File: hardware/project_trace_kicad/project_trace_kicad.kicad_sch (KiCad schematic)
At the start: 0 parts

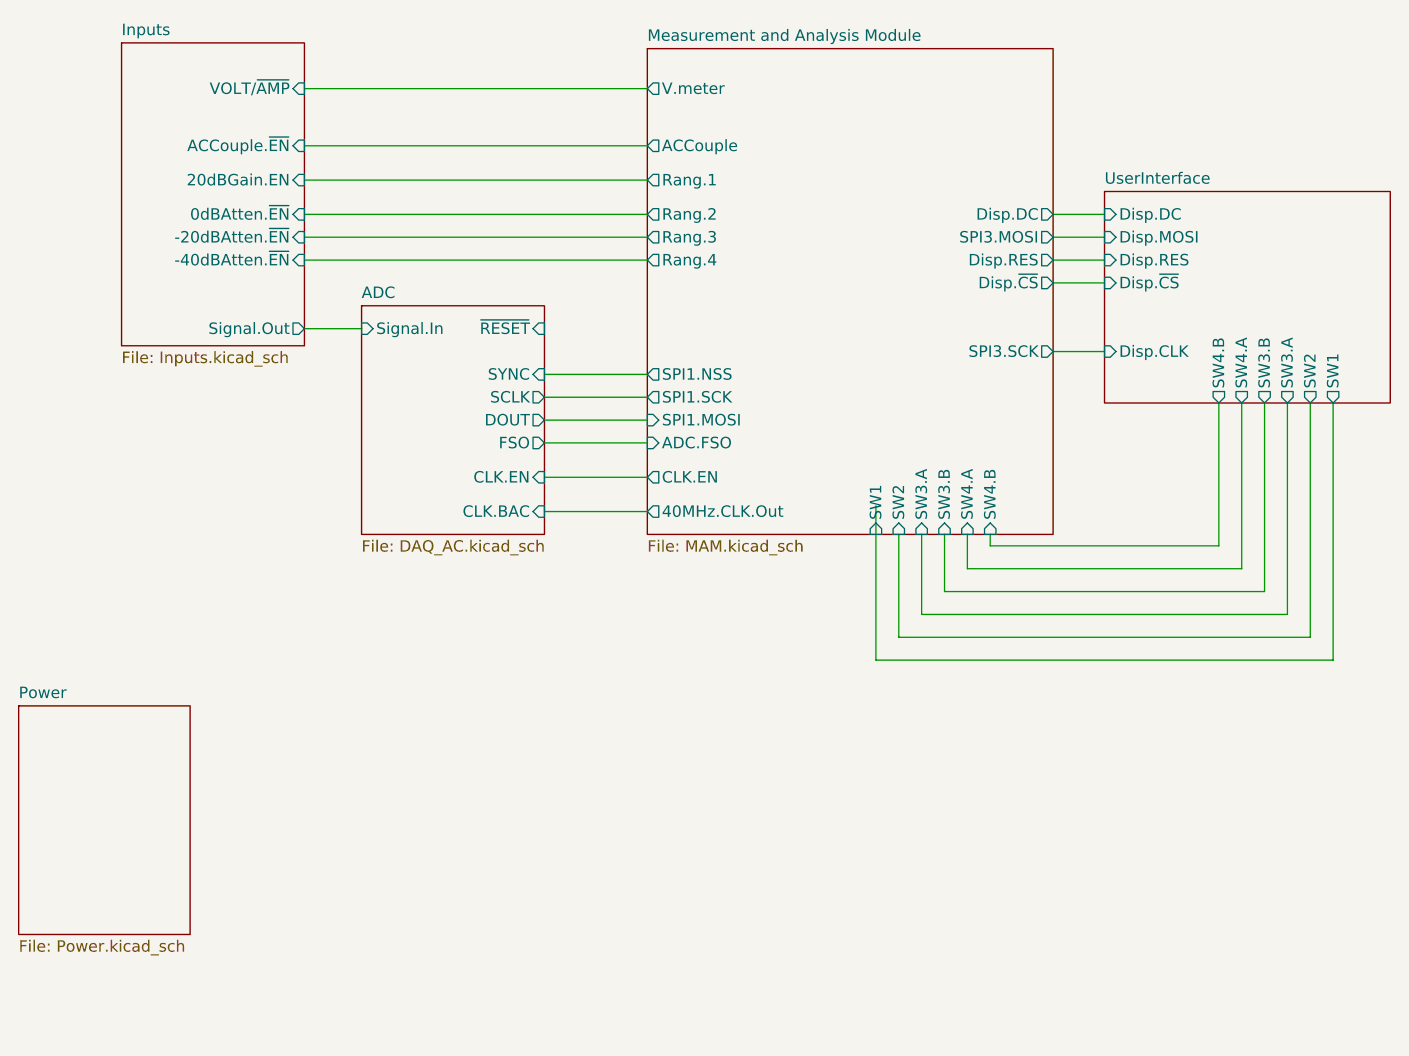
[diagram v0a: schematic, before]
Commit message: ERC Checks & Bug-Fixing
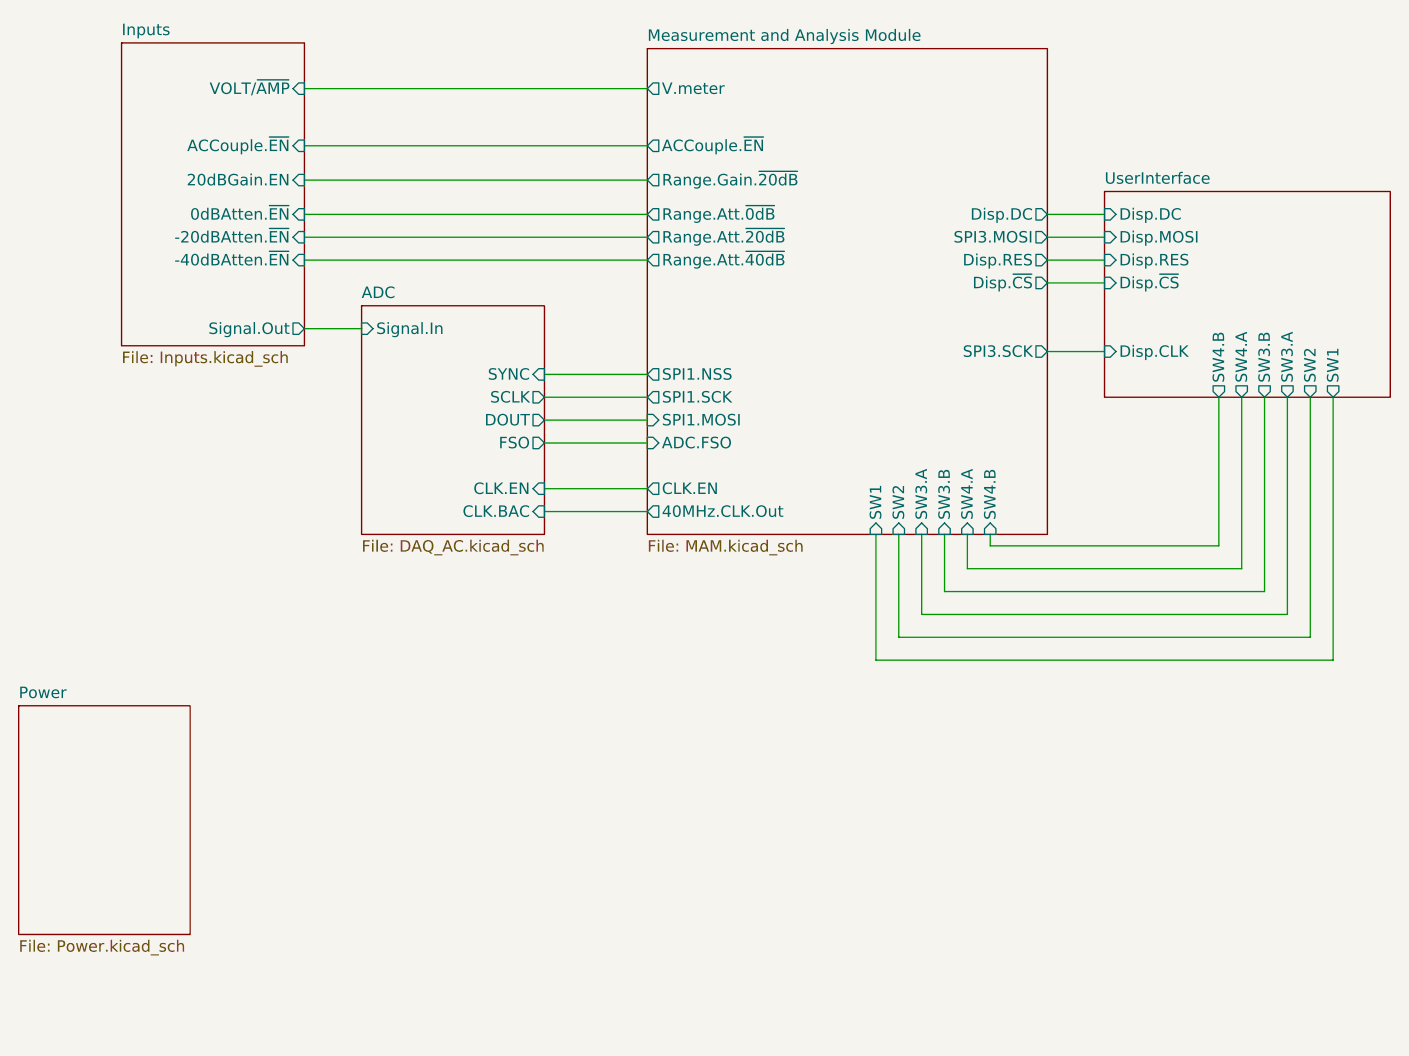
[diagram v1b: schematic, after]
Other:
- sheet ADC ports: added none; removed ~{RESET}
- sheet Measurement and Analysis Module ports: added ACCouple.~{EN}, Range.Att.~{0dB}, Range.Att.~{20dB}, Range.Att.~{40dB}, Range.Gain.~{20dB}; removed ACCouple, Rang.1, Rang.2, Rang.3, Rang.4
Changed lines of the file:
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@@
 	(wire
 		(pts
-			(xy 146.05 98.425) (xy 146.05 115.57)
-		)
-		(stroke
-			(width 0)
-			(type default)
-		)
-	)
-	(wire
-		(pts
-			(xy 109.22 95.25) (xy 120.65 95.25)
-		)
-		(stroke
-			(width 0)
-			(type default)
-		)
-	)
-	(wire
-		(pts
-			(xy 186.69 86.995) (xy 186.69 105.41)
+			(xy 146.05 101.6) (xy 146.05 115.57)
+		)
+		(stroke
+			(width 0)
+			(type default)
+		)
+	)
+	(wire
+		(pts
+			(xy 109.22 96.52) (xy 120.65 96.52)
+		)
+		(stroke
+			(width 0)
+			(type default)
+		)
+	)
+	(wire
+		(pts
+			(xy 186.69 86.36) (xy 186.69 105.41)
 		)
 		(stroke
@@
 	(wire
 		(pts
-			(xy 194.31 86.995) (xy 194.31 113.03)
+			(xy 194.31 86.36) (xy 194.31 113.03)
 		)
 		(stroke
@@
 	(wire
 		(pts
-			(xy 196.85 86.995) (xy 196.85 115.57)
-		)
-		(stroke
-			(width 0)
-			(type default)
-		)
-	)
-	(wire
-		(pts
-			(xy 165.735 81.28) (xy 171.45 81.28)
-		)
-		(stroke
-			(width 0)
-			(type default)
-		)
-	)
-	(wire
-		(pts
-			(xy 165.735 73.66) (xy 171.45 73.66)
-		)
-		(stroke
-			(width 0)
-			(type default)
-		)
-	)
-	(wire
-		(pts
-			(xy 191.77 86.995) (xy 191.77 110.49)
+			(xy 196.85 86.36) (xy 196.85 115.57)
+		)
+		(stroke
+			(width 0)
+			(type default)
+		)
+	)
+	(wire
+		(pts
+			(xy 165.1 81.28) (xy 171.45 81.28)
+		)
+		(stroke
+			(width 0)
+			(type default)
+		)
+	)
+	(wire
+		(pts
+			(xy 165.1 73.66) (xy 171.45 73.66)
+		)
+		(stroke
+			(width 0)
+			(type default)
+		)
+	)
+	(wire
+		(pts
+			(xy 191.77 86.36) (xy 191.77 110.49)
 		)
 		(stroke
@@
 	(wire
 		(pts
-			(xy 165.735 66.04) (xy 171.45 66.04)
+			(xy 165.1 66.04) (xy 171.45 66.04)
 		)
 		(stroke
@@
 	(wire
 		(pts
-			(xy 184.15 86.995) (xy 184.15 102.87)
+			(xy 184.15 86.36) (xy 184.15 102.87)
 		)
 		(stroke
@@
 	(wire
 		(pts
-			(xy 165.735 71.12) (xy 171.45 71.12)
-		)
-		(stroke
-			(width 0)
-			(type default)
-		)
-	)
-	(wire
-		(pts
-			(xy 165.735 68.58) (xy 171.45 68.58)
+			(xy 165.1 71.12) (xy 171.45 71.12)
+		)
+		(stroke
+			(width 0)
+			(type default)
+		)
+	)
+	(wire
+		(pts
+			(xy 165.1 68.58) (xy 171.45 68.58)
 		)
 		(stroke
@@
 	(wire
 		(pts
-			(xy 189.23 86.995) (xy 189.23 107.95)
+			(xy 189.23 86.36) (xy 189.23 107.95)
 		)
 		(stroke
@@
 	(sheet
 		(at 171.45 63.5)
-		(size 31.75 23.495)
+		(size 31.75 22.86)
 		(exclude_from_sim no)
 		(in_bom yes)
@@
 		)
 		(pin "SW1" output
-			(at 196.85 86.995 270)
+			(at 196.85 86.36 270)
 			(effects
 				(font
@@
 		)
 		(pin "SW2" output
-			(at 194.31 86.995 270)
+			(at 194.31 86.36 270)
 			(effects
 				(font
@@
 		)
 		(pin "SW3.A" output
-			(at 191.77 86.995 270)
+			(at 191.77 86.36 270)
 			(effects
 				(font
@@
 		)
 		(pin "SW3.B" output
-			(at 189.23 86.995 270)
+			(at 189.23 86.36 270)
 			(effects
 				(font
@@
 		)
 		(pin "SW4.A" output
-			(at 186.69 86.995 270)
+			(at 186.69 86.36 270)
 			(effects
 				(font
@@
 		)
 		(pin "SW4.B" output
-			(at 184.15 86.995 270)
+			(at 184.15 86.36 270)
 			(effects
 				(font
@@
 			)
 		)
-		(pin "~{RESET}" input
-			(at 109.22 78.74 0)
-			(effects
-				(font
-					(size 1.27 1.27)
-				)
-				(justify right)
-			)
-		)
 		(pin "CLK.BAC" input
 			(at 109.22 99.06 0)
@@
 		)
 		(pin "CLK.EN" input
-			(at 109.22 95.25 0)
+			(at 109.22 96.52 0)
 			(effects
 				(font
@@
 	(sheet
 		(at 120.65 47.625)
-		(size 45.085 53.975)
+		(size 44.45 53.975)
 		(exclude_from_sim no)
 		(in_bom yes)
@@
 		)
 		(pin "Disp.DC" output
-			(at 165.735 66.04 0)
+			(at 165.1 66.04 0)
 			(effects
 				(font
@@
 		)
 		(pin "Disp.RES" output
-			(at 165.735 71.12 0)
+			(at 165.1 71.12 0)
 			(effects
 				(font
@@
 		)
 		(pin "Disp.~{CS}" output
-			(at 165.735 73.66 0)
+			(at 165.1 73.66 0)
 			(effects
 				(font
@@
 		)
 		(pin "SPI3.MOSI" output
-			(at 165.735 68.58 0)
+			(at 165.1 68.58 0)
 			(effects
 				(font
@@
 		)
 		(pin "SPI3.SCK" output
-			(at 165.735 81.28 0)
-			(effects
-				(font
-					(size 1.27 1.27)
-				)
-				(justify right)
-			)
-		)
-		(pin "ACCouple" output
-			(at 120.65 58.42 180)
-			(effects
-				(font
-					(size 1.27 1.27)
-				)
-				(justify left)
-			)
-		)
-		(pin "Rang.1" output
-			(at 120.65 62.23 180)
-			(effects
-				(font
-					(size 1.27 1.27)
-				)
-				(justify left)
-			)
-		)
-		(pin "Rang.2" output
-			(at 120.65 66.04 180)
-			(effects
-				(font
-					(size 1.27 1.27)
-				)
-				(justify left)
-			)
-		)
-		(pin "Rang.3" output
-			(at 120.65 68.58 180)
-			(effects
-				(font
-					(size 1.27 1.27)
-				)
-				(justify left)
-			)
-		)
-		(pin "Rang.4" output
-			(at 120.65 71.12 180)
-			(effects
-				(font
-					(size 1.27 1.27)
-				)
-				(justify left)
+			(at 165.1 81.28 0)
+			(effects
+				(font
+					(size 1.27 1.27)
+				)
+				(justify right)
 			)
 		)
@@
 		)
 		(pin "CLK.EN" output
-			(at 120.65 95.25 180)
-			(effects
-				(font
+			(at 120.65 96.52 180)
+			(effects
+				(font
+					(size 1.27 1.27)
+				)
+				(justify left)
+			)
+		)
+		(pin "ACCouple.~{EN}" output
+			(at 120.65 58.42 180)
+			(effects
+				(font
+					(size 1.27 1.27)
+				)
+				(justify left)
+			)
+		)
+		(pin "Range.Att.~{0dB}" output
+			(at 120.65 66.04 180)
+			(effects
+				(font
+					(size 1.27 1.27)
+				)
+				(justify left)
+			)
+		)
+		(pin "Range.Att.~{20dB}" output
+			(at 120.65 68.58 180)
+			(effects
+				(font
+					(size 1.27 1.27)
+				)
+				(justify left)
+			)
+		)
+		(pin "Range.Att.~{40dB}" output
+			(at 120.65 71.12 180)
+			(effects
+				(font
+					(size 1.27 1.27)
+				)
+				(justify left)
+			)
+		)
+		(pin "Range.Gain.~{20dB}" output
+			(at 120.65 62.23 180)
+			(effects
+				(font

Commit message: Fix inconsistency with ADC datasheet, fix DRC Errors
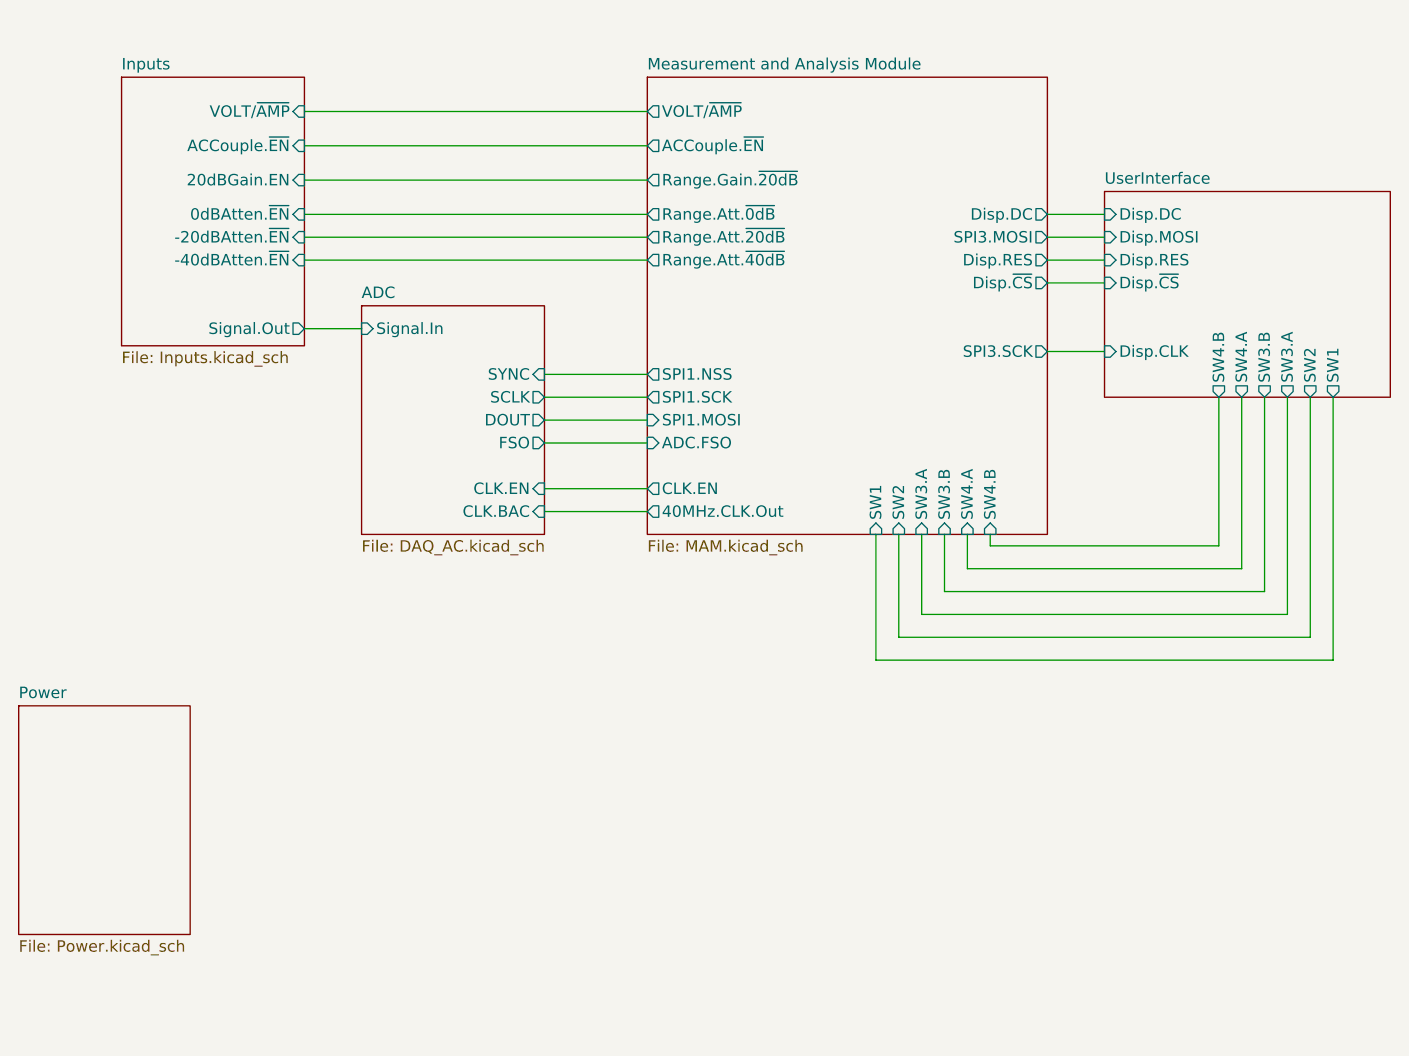
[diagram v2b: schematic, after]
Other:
- sheet Measurement and Analysis Module ports: added VOLT/~{AMP}; removed V.meter
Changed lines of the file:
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@@
 	(wire
 		(pts
-			(xy 82.55 52.07) (xy 120.65 52.07)
+			(xy 82.55 54.61) (xy 120.65 54.61)
 		)
 		(stroke
@@
 	)
 	(sheet
-		(at 62.23 46.99)
-		(size 20.32 33.655)
+		(at 62.23 50.8)
+		(size 20.32 29.845)
 		(exclude_from_sim no)
 		(in_bom yes)
@@
 		)
 		(property "Sheetname" "Inputs"
-			(at 62.23 46.2784 0)
+			(at 62.23 50.0884 0)
 			(show_name no)
 			(do_not_autoplace no)
@@
 		)
 		(pin "VOLT{slash}~{AMP}" input
-			(at 82.55 52.07 0)
+			(at 82.55 54.61 0)
 			(effects
 				(font
@@
 	)
 	(sheet
-		(at 120.65 47.625)
-		(size 44.45 53.975)
+		(at 120.65 50.8)
+		(size 44.45 50.8)
 		(exclude_from_sim no)
 		(in_bom yes)
@@
 		)
 		(property "Sheetname" "Measurement and Analysis Module"
-			(at 120.65 46.9134 0)
+			(at 120.65 50.0884 0)
 			(show_name no)
 			(do_not_autoplace no)
@@
 			)
 		)
-		(pin "V.meter" output
-			(at 120.65 52.07 180)
-			(effects
-				(font
-					(size 1.27 1.27)
-				)
-				(justify left)
-			)
-		)
 		(pin "40MHz.CLK.Out" output
 			(at 120.65 99.06 180)
@@
 			(effects
 				(font
+					(size 1.27 1.27)
+				)
+				(justify left)
+			)
+		)
+		(pin "VOLT{slash}~{AMP}" output
+			(at 120.65 54.61 180)
+			(effects
+				(font

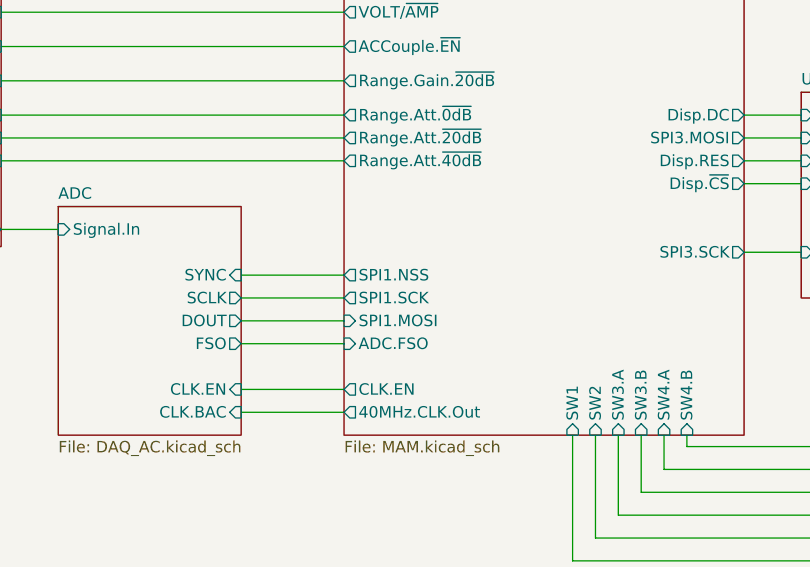
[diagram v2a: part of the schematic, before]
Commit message: Hardware NSS renamed to SYNC
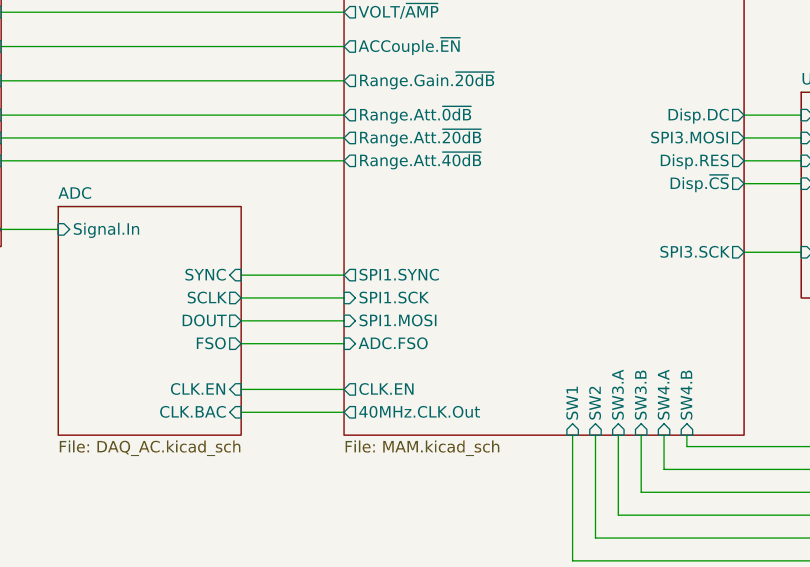
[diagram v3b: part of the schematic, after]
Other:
- sheet Measurement and Analysis Module ports: added SPI1.SYNC; removed SPI1.NSS
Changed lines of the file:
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@@
 			)
 		)
-		(pin "SPI1.NSS" output
+		(pin "SPI1.SYNC" output
 			(at 120.65 83.82 180)
 			(effects
@@
 			)
 		)
-		(pin "SPI1.SCK" output
+		(pin "SPI1.SCK" input
 			(at 120.65 86.36 180)
 			(effects
